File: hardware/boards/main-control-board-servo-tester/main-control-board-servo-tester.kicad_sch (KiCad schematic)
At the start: 5 parts, among them J1 Conn_01x03_Socket

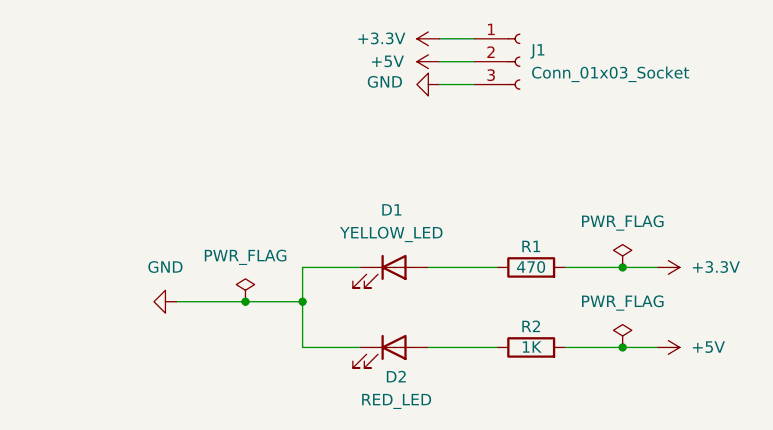
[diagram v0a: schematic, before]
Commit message: fix(pcb): update net names and adjust component placements for improved layout
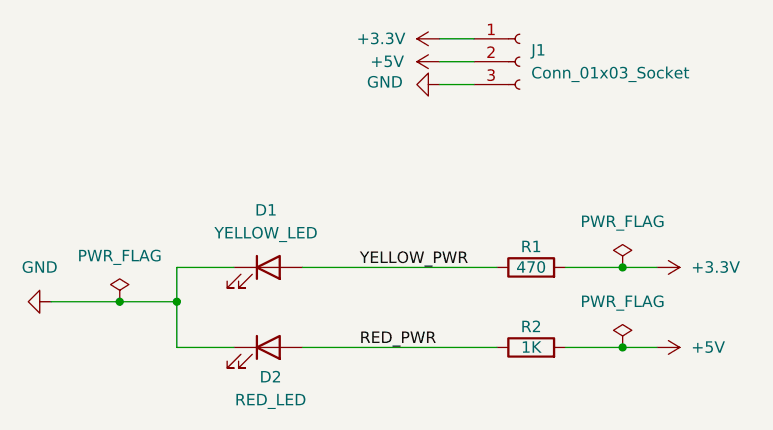
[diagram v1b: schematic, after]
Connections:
- net RED_PWR: now reaches D2.2 (A), R2.1
- net YELLOW_PWR: now reaches D1.2 (A), R1.1
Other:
- moved on the sheet: D1, D2
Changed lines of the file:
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@@
 	)
 	(junction
-		(at 106.68 110.49)
+		(at 92.71 110.49)
 		(diameter 0)
 		(color 0 0 0 0)
@@
 	)
 	(junction
-		(at 113.03 110.49)
+		(at 99.06 110.49)
 		(diameter 0)
 		(color 0 0 0 0)
@@
 	(wire
 		(pts
-			(xy 113.03 115.57) (xy 113.03 110.49)
-		)
-		(stroke
-			(width 0)
-			(type default)
-		)
-	)
-	(wire
-		(pts
-			(xy 113.03 110.49) (xy 113.03 106.68)
+			(xy 99.06 115.57) (xy 99.06 110.49)
+		)
+		(stroke
+			(width 0)
+			(type default)
+		)
+	)
+	(wire
+		(pts
+			(xy 99.06 110.49) (xy 99.06 106.68)
 		)
 		(stroke
@@
 	(wire
 		(pts
-			(xy 99.06 110.49) (xy 113.03 110.49)
-		)
-		(stroke
-			(width 0)
-			(type default)
-		)
-	)
-	(wire
-		(pts
-			(xy 113.03 106.68) (xy 119.38 106.68)
-		)
-		(stroke
-			(width 0)
-			(type default)
-		)
-	)
-	(wire
-		(pts
-			(xy 119.38 115.57) (xy 113.03 115.57)
+			(xy 85.09 110.49) (xy 99.06 110.49)
+		)
+		(stroke
+			(width 0)
+			(type default)
+		)
+	)
+	(wire
+		(pts
+			(xy 99.06 106.68) (xy 105.41 106.68)
+		)
+		(stroke
+			(width 0)
+			(type default)
+		)
+	)
+	(wire
+		(pts
+			(xy 105.41 115.57) (xy 99.06 115.57)
 		)
 		(stroke
@@
 	(wire
 		(pts
-			(xy 127 106.68) (xy 134.62 106.68)
+			(xy 113.03 106.68) (xy 134.62 106.68)
 		)
 		(stroke
@@
 	(wire
 		(pts
-			(xy 127 115.57) (xy 134.62 115.57)
-		)
-		(stroke
-			(width 0)
-			(type default)
+			(xy 113.03 115.57) (xy 134.62 115.57)
+		)
+		(stroke
+			(width 0)
+			(type default)
+		)
+	)
+	(label "RED_PWR"
+		(at 119.38 115.57 0)
+		(effects
+			(font
+				(size 1.27 1.27)
+			)
+			(justify left bottom)
+		)
+	)
+	(label "YELLOW_PWR"
+		(at 119.38 106.68 0)
+		(effects
+			(font
+				(size 1.27 1.27)
+			)
+			(justify left bottom)
 		)
 	)
@@
 	(symbol
 		(lib_id "power:PWR_FLAG")
-		(at 106.68 110.49 0)
+		(at 92.71 110.49 0)
 		(unit 1)
 		(body_style 1)
@@
 		(fields_autoplaced yes)
 		(property "Reference" "#FLG03"
-			(at 106.68 108.585 0)
+			(at 92.71 108.585 0)
 			(hide yes)
 			(show_name no)
@@
 		)
 		(property "Value" "PWR_FLAG"
-			(at 106.68 105.41 0)
+			(at 92.71 105.41 0)
 			(show_name no)
 			(do_not_autoplace no)
@@
 		)
 		(property "Footprint" ""
-			(at 106.68 110.49 0)
+			(at 92.71 110.49 0)
 			(hide yes)
 			(show_name no)
@@
 		)
 		(property "Datasheet" ""
-			(at 106.68 110.49 0)
+			(at 92.71 110.49 0)
 			(hide yes)
 			(show_name no)
@@
 		)
 		(property "Description" "Special symbol for telling ERC where power comes from"
-			(at 106.68 110.49 0)
+			(at 92.71 110.49 0)
 			(hide yes)
 			(show_name no)
@@
 	(symbol
 		(lib_id "power:GND")
-		(at 99.06 110.49 270)
+		(at 85.09 110.49 270)
 		(unit 1)
 		(body_style 1)
@@
 		(fields_autoplaced yes)
 		(property "Reference" "#PWR03"
-			(at 92.71 110.49 0)
+			(at 78.74 110.49 0)
 			(hide yes)
 			(show_name no)
@@
 		)
 		(property "Value" "GND"
-			(at 97.79 106.68 90)
+			(at 83.82 106.68 90)
 			(show_name no)
 			(do_not_autoplace no)
@@
 		)
 		(property "Footprint" ""
-			(at 99.06 110.49 0)
+			(at 85.09 110.49 0)
 			(hide yes)
 			(show_name no)
@@
 		)
 		(property "Datasheet" ""
-			(at 99.06 110.49 0)
+			(at 85.09 110.49 0)
 			(hide yes)
 			(show_name no)
@@
 		)
 		(property "Description" "Power symbol creates a global label with name \"GND\" , ground"
-			(at 99.06 110.49 0)
+			(at 85.09 110.49 0)
 			(hide yes)
 			(show_name no)
@@
 	(symbol
 		(lib_id "Device:LED")
-		(at 123.19 106.68 0)
+		(at 109.22 106.68 0)
 		(unit 1)
 		(body_style 1)
@@
 		(dnp no)
 		(property "Reference" "D1"
-			(at 122.936 100.33 0)
+			(at 108.966 100.33 0)
 			(show_name no)
 			(do_not_autoplace no)
@@
 		)
 		(property "Value" "YELLOW_LED"
-			(at 122.936 102.87 0)
+			(at 108.966 102.87 0)
 			(show_name no)
 			(do_not_autoplace no)
@@
 		)
 		(property "Footprint" "LED_SMD:LED_0603_1608Metric"
-			(at 123.19 106.68 0)
+			(at 109.22 106.68 0)
 			(hide yes)
 			(show_name no)
@@
 		)
 		(property "Datasheet" ""
-			(at 123.19 106.68 0)
+			(at 109.22 106.68 0)
 			(hide yes)
 			(show_name no)
@@
 		)
 		(property "Description" "Light emitting diode"
-			(at 123.19 106.68 0)
+			(at 109.22 106.68 0)
 			(hide yes)
 			(show_name no)
@@
 		)
 		(property "Sim.Pins" "1=K 2=A"
-			(at 123.19 106.68 0)
+			(at 109.22 106.68 0)
 			(hide yes)
 			(show_name no)
@@
 		)
 		(property "LCSC Part #" "C2287"
-			(at 123.19 106.68 0)
+			(at 109.22 106.68 0)
 			(hide yes)
 			(show_name no)
@@
 		)
 		(property "MPN" "KT-0603Y"
-			(at 123.19 106.68 0)
+			(at 109.22 106.68 0)
 			(hide yes)
 			(show_name no)
@@
 		)
 		(property "Manufacturer" "Hubei KENTO Elec"
-			(at 123.19 106.68 0)
+			(at 109.22 106.68 0)
 			(hide yes)
 			(show_name no)
@@
 	(symbol
 		(lib_id "Device:LED")
-		(at 123.19 115.57 0)
+		(at 109.22 115.57 0)
 		(unit 1)
 		(body_style 1)
@@
 		(dnp no)
 		(property "Reference" "D2"
-			(at 123.444 118.872 0)
+			(at 109.474 118.872 0)
 			(show_name no)
 			(do_not_autoplace no)
@@
 		)
 		(property "Value" "RED_LED"
-			(at 123.444 121.412 0)
+			(at 109.474 121.412 0)
 			(show_name no)
 			(do_not_autoplace no)
@@
 		)
 		(property "Footprint" "LED_SMD:LED_0603_1608Metric"
-			(at 123.19 115.57 0)
+			(at 109.22 115.57 0)
 			(hide yes)
 			(show_name no)
@@
 		)
 		(property "Datasheet" ""
-			(at 123.19 115.57 0)
+			(at 109.22 115.57 0)
 			(hide yes)
 			(show_name no)
@@
 		)
 		(property "Description" "Light emitting diode"
-			(at 123.19 115.57 0)
+			(at 109.22 115.57 0)
 			(hide yes)
 			(show_name no)
@@
 		)
 		(property "Sim.Pins" "1=K 2=A"
-			(at 123.19 115.57 0)
+			(at 109.22 115.57 0)
 			(hide yes)
 			(show_name no)
@@
 		)
 		(property "LCSC Part #" "C2286"
-			(at 123.19 115.57 0)
+			(at 109.22 115.57 0)
 			(hide yes)
 			(show_name no)
@@
 		)
 		(property "MPN" "KT-0603R"
-			(at 123.19 115.57 0)
+			(at 109.22 115.57 0)
 			(hide yes)
 			(show_name no)
@@
 		)
 		(property "Manufacturer" "Hubei KENTO Elec"
-			(at 123.19 115.57 0)
-			(hide yes)
-			(show_name no)
+			(at 109.22 115.57 0)
+			(hide yes)
+			(show_name no)

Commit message: fix(pcb): update LCSC Part # and MPN for component accuracy
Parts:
- R2: LCSC Part # 0603WAF1001T5E -> C21190; MPN C21190 -> 0603WAF1001T5E
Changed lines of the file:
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@@
 			)
 		)
-		(property "LCSC Part #" "0603WAF1001T5E"
+		(property "LCSC Part #" "C21190"
 			(at 138.43 115.57 90)
 			(hide yes)
@@
 			)
 		)
-		(property "MPN" "C21190"
+		(property "MPN" "0603WAF1001T5E"
 			(at 138.43 115.57 90)
 			(hide yes)

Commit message: fix(pcb): update component properties and adjust silk screen text for clarity
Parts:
- J1: FT Rotation Offset (none) -> -90
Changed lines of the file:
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@@
+			)
+		)
+		(property "FT Rotation Offset" "-90"
+			(at 137.16 83.82 0)
+			(hide yes)
+			(show_name no)
+			(do_not_autoplace no)
+			(effects
+				(font
+					(size 1.27 1.27)
+				)
 			)
 		)
